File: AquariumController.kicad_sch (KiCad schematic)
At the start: 16 parts, among them J1 Temp_1_Screw_Terminal, J2 Temp_2_Screw_Terminal, J3 12V_Output_1_Screw_Terminal, J4 12V_Output_2_Screw_Terminal, J5 Input_1_Screw_Terminal, J6 Input_2_Screw_Terminal, J7 IR_LED_Screw_Terminal, J8 Conn_01x02, Q1 IRF3708, Q2 IRF3708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

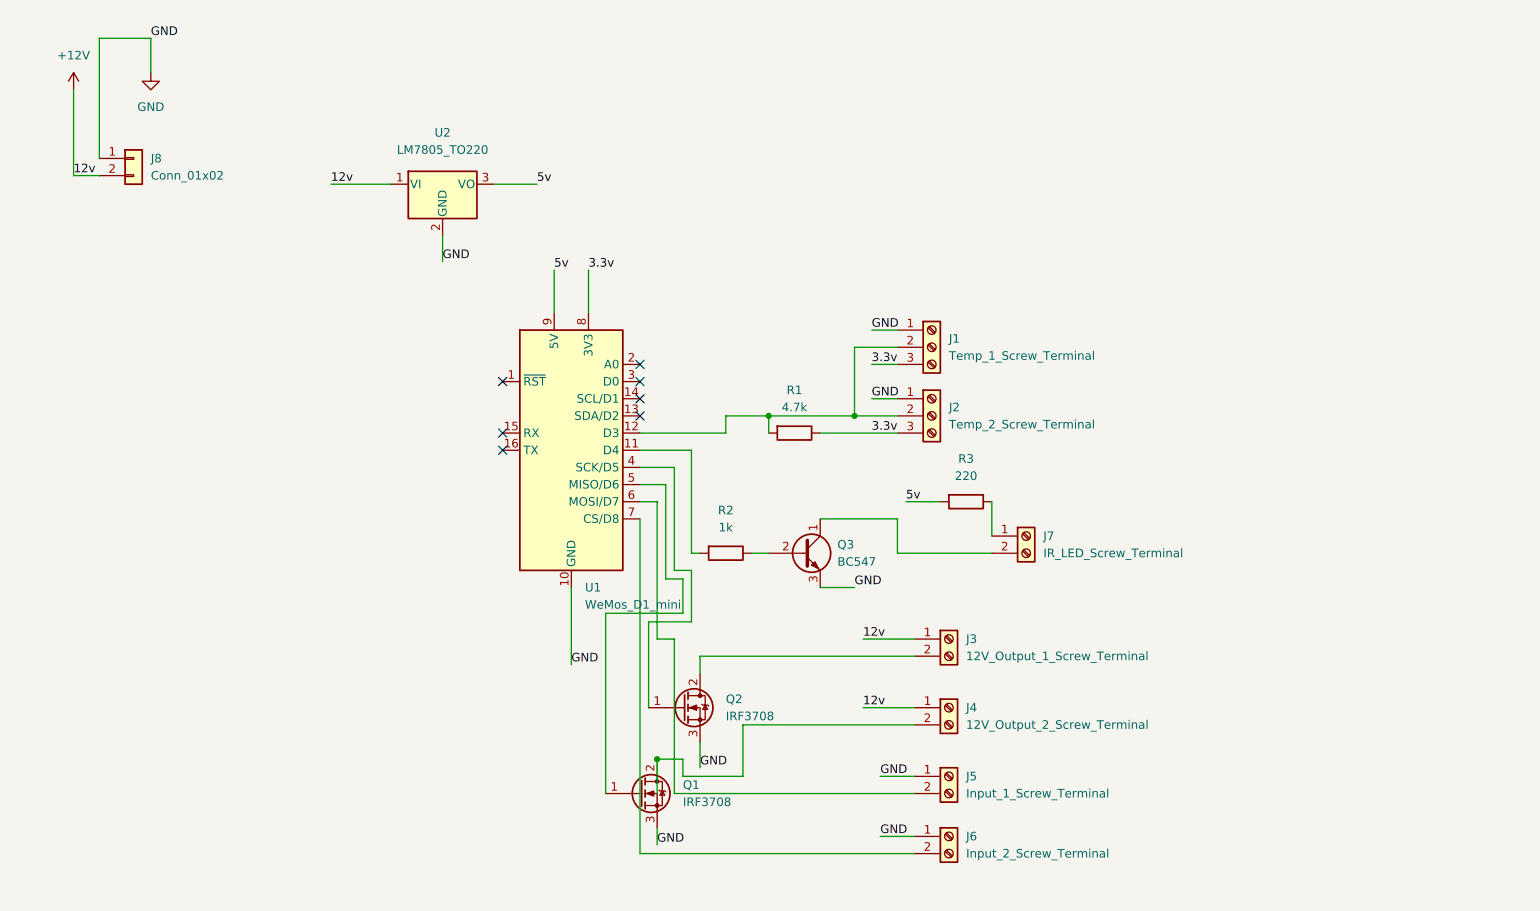
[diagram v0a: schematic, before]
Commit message: Swap out all the mosfets/bjts add the i2c breakout flip the power to the right side
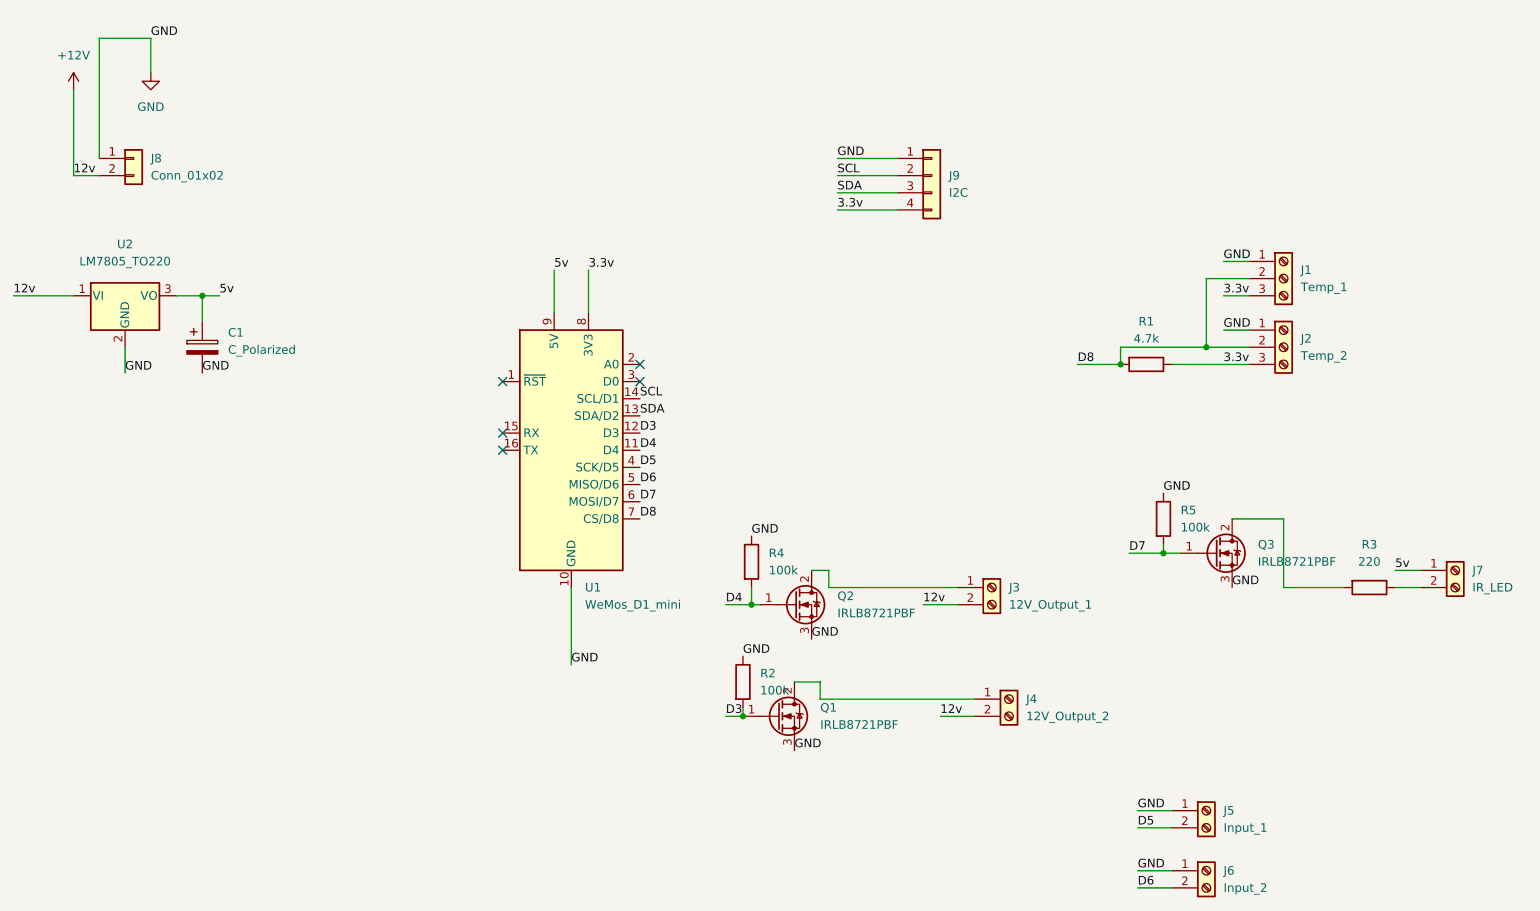
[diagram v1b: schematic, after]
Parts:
- removed Q1, Q2: IRF3708, Package_TO_SOT_THT:TO-220-3_Vertical, symbol Transistor_FET:IRF3205
- removed Q3: BC547, Package_TO_SOT_THT:TO-92_Inline, symbol Transistor_BJT:BC547
- added C1: C_Polarized, Capacitor_THT:C_Radial_D5.0mm_H11.0mm_P2.00mm, symbol Device:C_Polarized
- added J9: I2C, Connector_JST:JST_XH_S4B-XH-A_1x04_P2.50mm_Horizontal, symbol Connector_Generic:Conn_01x04
- added Q1, Q2, Q3: IRLB8721PBF, Package_TO_SOT_THT:TO-220-3_Vertical, symbol Transistor_FET:IRLB8721PBF
- added R4, R5: 100k, Resistor_THT:R_Axial_DIN0207_L6.3mm_D2.5mm_P10.16mm_Horizontal, symbol Device:R
- J1: value Temp_1_Screw_Terminal -> Temp_1; footprint TerminalBlock_RND:TerminalBlock_RND_205-00002_1x03_P5.00mm_Horizontal -> TerminalBlock_Phoenix:TerminalBlock_Phoenix_MKDS-1,5-3-5.08_1x03_P5.08mm_Horizontal
- J2: value Temp_2_Screw_Terminal -> Temp_2; footprint TerminalBlock_RND:TerminalBlock_RND_205-00002_1x03_P5.00mm_Horizontal -> TerminalBlock_Phoenix:TerminalBlock_Phoenix_MKDS-1,5-3-5.08_1x03_P5.08mm_Horizontal
- J3: value 12V_Output_1_Screw_Terminal -> 12V_Output_1; footprint TerminalBlock_RND:TerminalBlock_RND_205-00001_1x02_P5.00mm_Horizontal -> TerminalBlock_Phoenix:TerminalBlock_Phoenix_MKDS-1,5-2-5.08_1x02_P5.08mm_Horizontal
- J4: value 12V_Output_2_Screw_Terminal -> 12V_Output_2; footprint TerminalBlock_RND:TerminalBlock_RND_205-00001_1x02_P5.00mm_Horizontal -> TerminalBlock_Phoenix:TerminalBlock_Phoenix_MKDS-1,5-2-5.08_1x02_P5.08mm_Horizontal
- J5: value Input_1_Screw_Terminal -> Input_1; footprint TerminalBlock_RND:TerminalBlock_RND_205-00001_1x02_P5.00mm_Horizontal -> TerminalBlock_Phoenix:TerminalBlock_Phoenix_MKDS-1,5-2-5.08_1x02_P5.08mm_Horizontal
- J6: value Input_2_Screw_Terminal -> Input_2; footprint TerminalBlock_RND:TerminalBlock_RND_205-00001_1x02_P5.00mm_Horizontal -> TerminalBlock_Phoenix:TerminalBlock_Phoenix_MKDS-1,5-2-5.08_1x02_P5.08mm_Horizontal
- J7: value IR_LED_Screw_Terminal -> IR_LED; footprint TerminalBlock_RND:TerminalBlock_RND_205-00001_1x02_P5.00mm_Horizontal -> TerminalBlock_Phoenix:TerminalBlock_Phoenix_MKDS-1,5-2-5.08_1x02_P5.08mm_Horizontal
- J8: footprint Connector_JST:JST_XH_B2B-XH-AM_1x02_P2.50mm_Vertical -> Connector_JST:JST_XH_B2B-XH-A_1x02_P2.50mm_Vertical
- R1, R3: footprint Resistor_THT:R_Axial_DIN0207_L6.3mm_D2.5mm_P15.24mm_Horizontal -> Resistor_THT:R_Axial_DIN0207_L6.3mm_D2.5mm_P10.16mm_Horizontal
- R2: value 1k -> 100k; footprint Resistor_THT:R_Axial_DIN0207_L6.3mm_D2.5mm_P15.24mm_Horizontal -> Resistor_THT:R_Axial_DIN0207_L6.3mm_D2.5mm_P10.16mm_Horizontal
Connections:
- net +12V: now also J3.2 (Pin_2), J4.2 (Pin_2); no longer J3.1 (Pin_1), J4.1 (Pin_1)
- net 3.3v: now also J9.4 (Pin_4)
- net 5v: now also J7.1 (Pin_1), C1.1; no longer R3.2
- net GND: now also R2.1, C1.2, J9.1 (Pin_1), Q1.3 (S), Q2.3 (S), Q3.3 (S), R4.1, R5.1
- net at J7.2 (Pin_2): now also R3.1
- net D6: now reaches J6.2 (Pin_2)
- net D6: now also U1.5 (MISO/D6); no longer U1.7 (CS/D8)
- net D8: now reaches J1.2 (Pin_2), J2.2 (Pin_2), R1.2
- net D8: now also U1.7 (CS/D8); no longer U1.12 (D3)
- net D5: now reaches J5.2 (Pin_2)
- net D5: now also U1.4 (SCK/D5); no longer U1.6 (MOSI/D7)
- net D3: now reaches R2.2
- net D3: now also U1.12 (D3), Q1.1 (G); no longer U1.11 (D4)
- net SDA: now reaches U1.13 (SDA/D2)
- net SDA: now also J9.3 (Pin_3)
- net SCL: now reaches U1.14 (SCL/D1)
- net SCL: now also J9.2 (Pin_2)
- new net: Q3.2 (D), R3.2
- new net: J4.1 (Pin_1), Q1.2 (D)
- new net: J3.1 (Pin_1), Q2.2 (D)
- new net D4: Q2.1 (G), R4.2, U1.11 (D4)
- new net D7: Q3.1 (G), R5.2, U1.6 (MOSI/D7)
- no-connect marks 7 -> 5
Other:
- moved on the sheet: J1, J2, J3, J4, J5, J6, J7, R1, R3, U2

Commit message: make the holes not on the schematic and fix the name of the 12v input
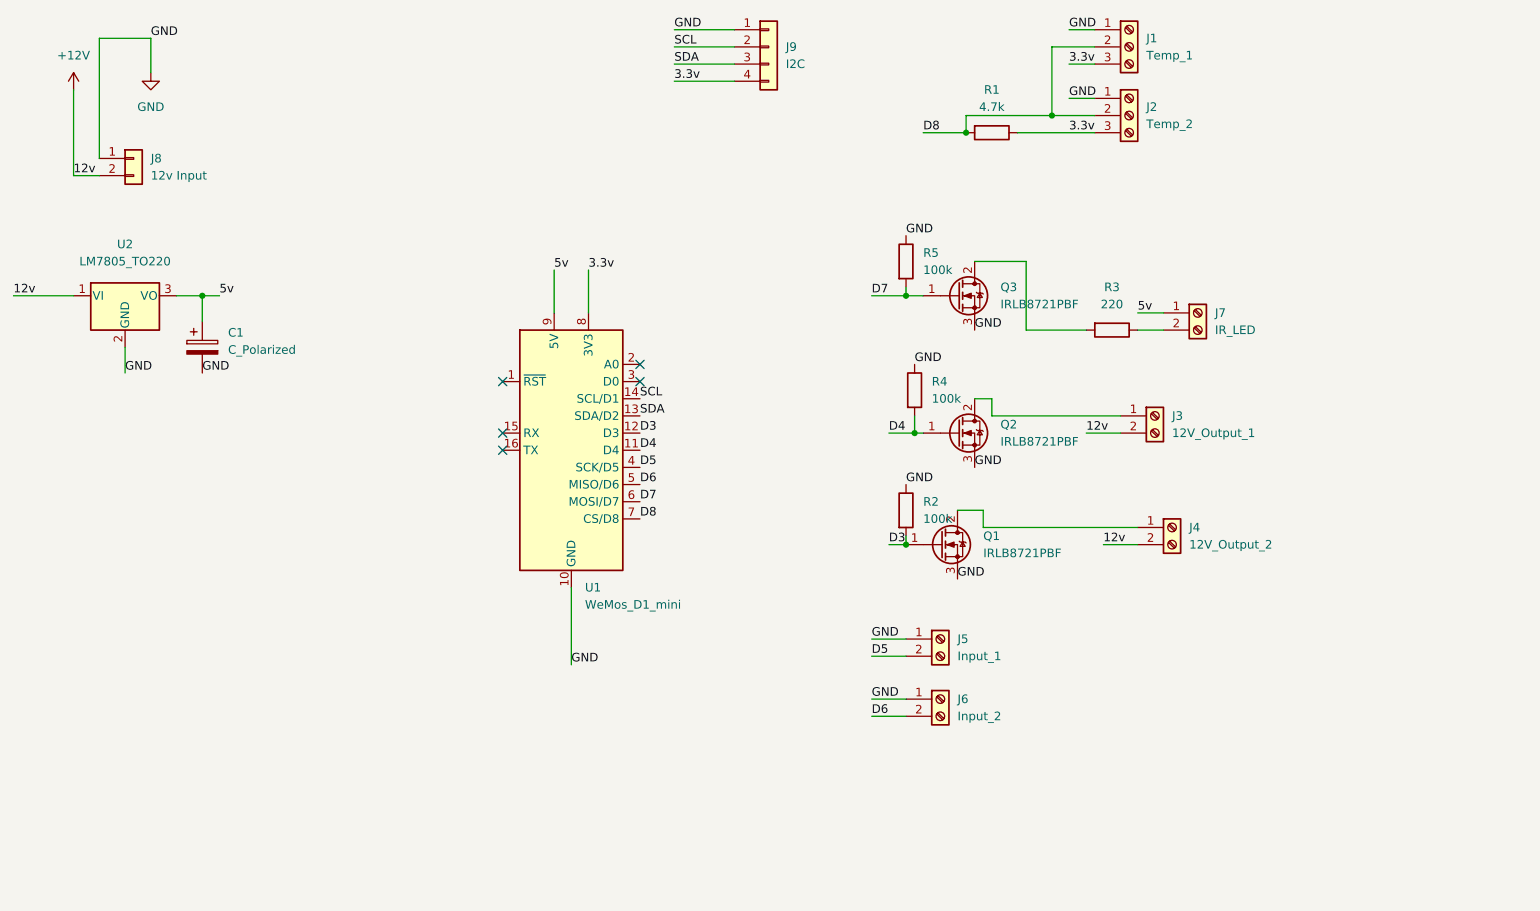
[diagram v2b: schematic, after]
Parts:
- J8: value Conn_01x02 -> 12v Input
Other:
- title: (none) -> Basic Aquarium Controller
- moved on the sheet: J1, J2, J3, J4, J5, J6, J7, J9, Q1, Q2, Q3, R1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
